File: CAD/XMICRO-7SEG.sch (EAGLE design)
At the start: 67 parts, among them U1 GAL16V8B, U10 74244, U11 74245, U2 GAL16V8B, U3 GAL16V8B, U4 GAL16V8B, U5 74273, U6 74273, U7 74138, U8 74138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

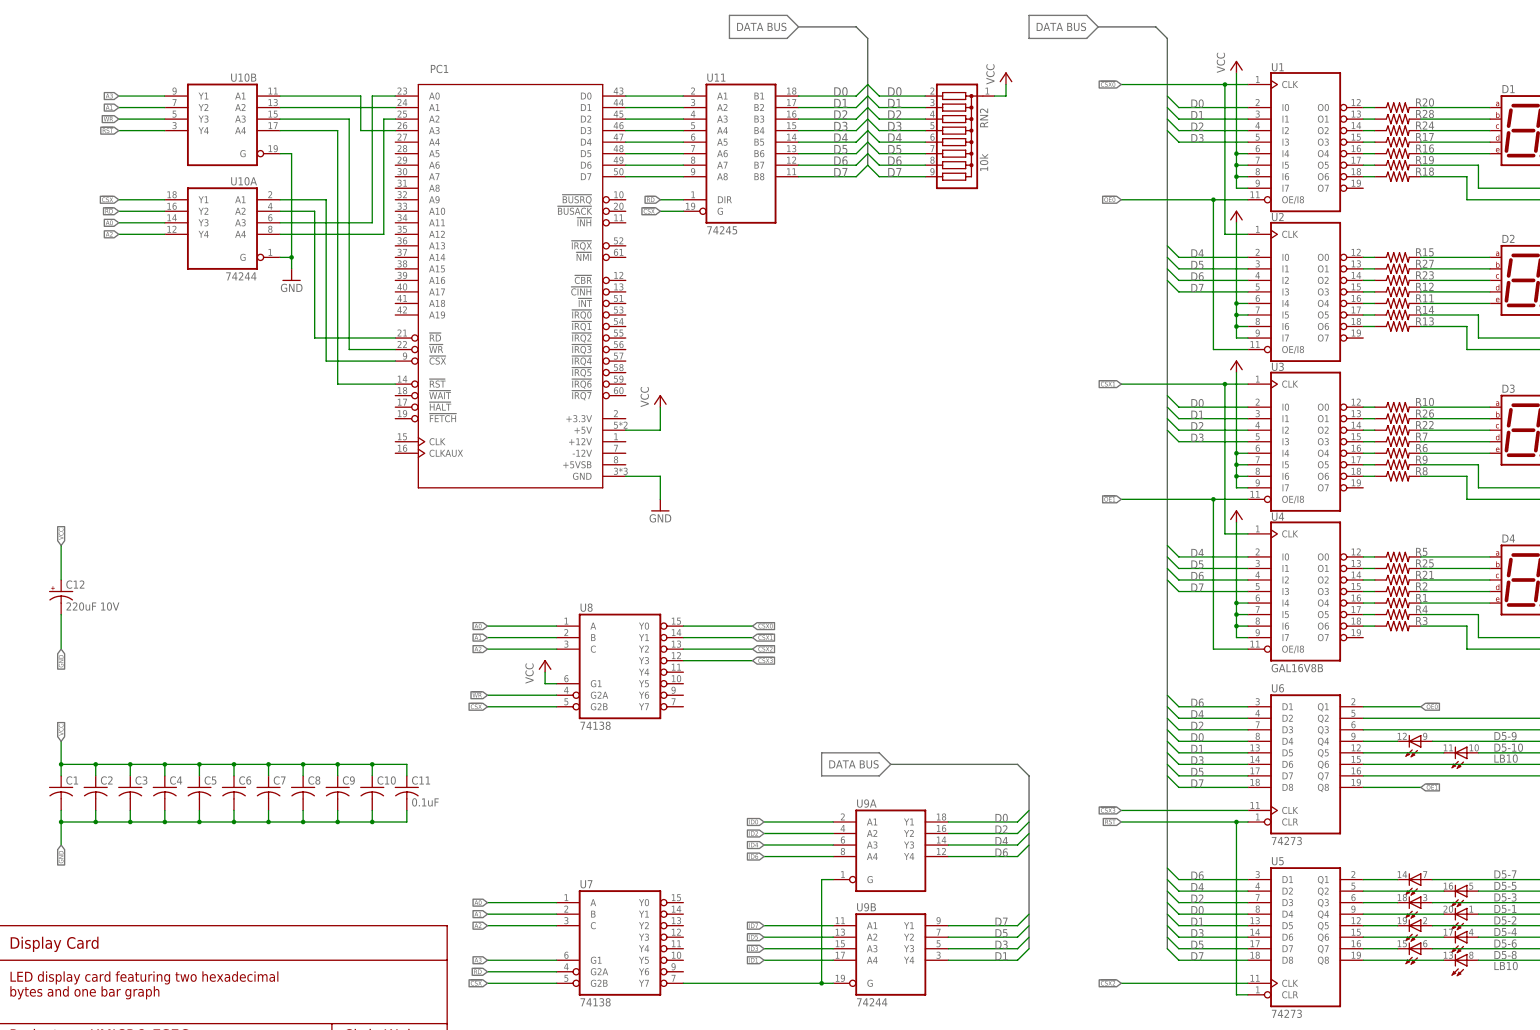
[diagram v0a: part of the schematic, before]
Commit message: Updated schematic xrefs to indicate signal direction.
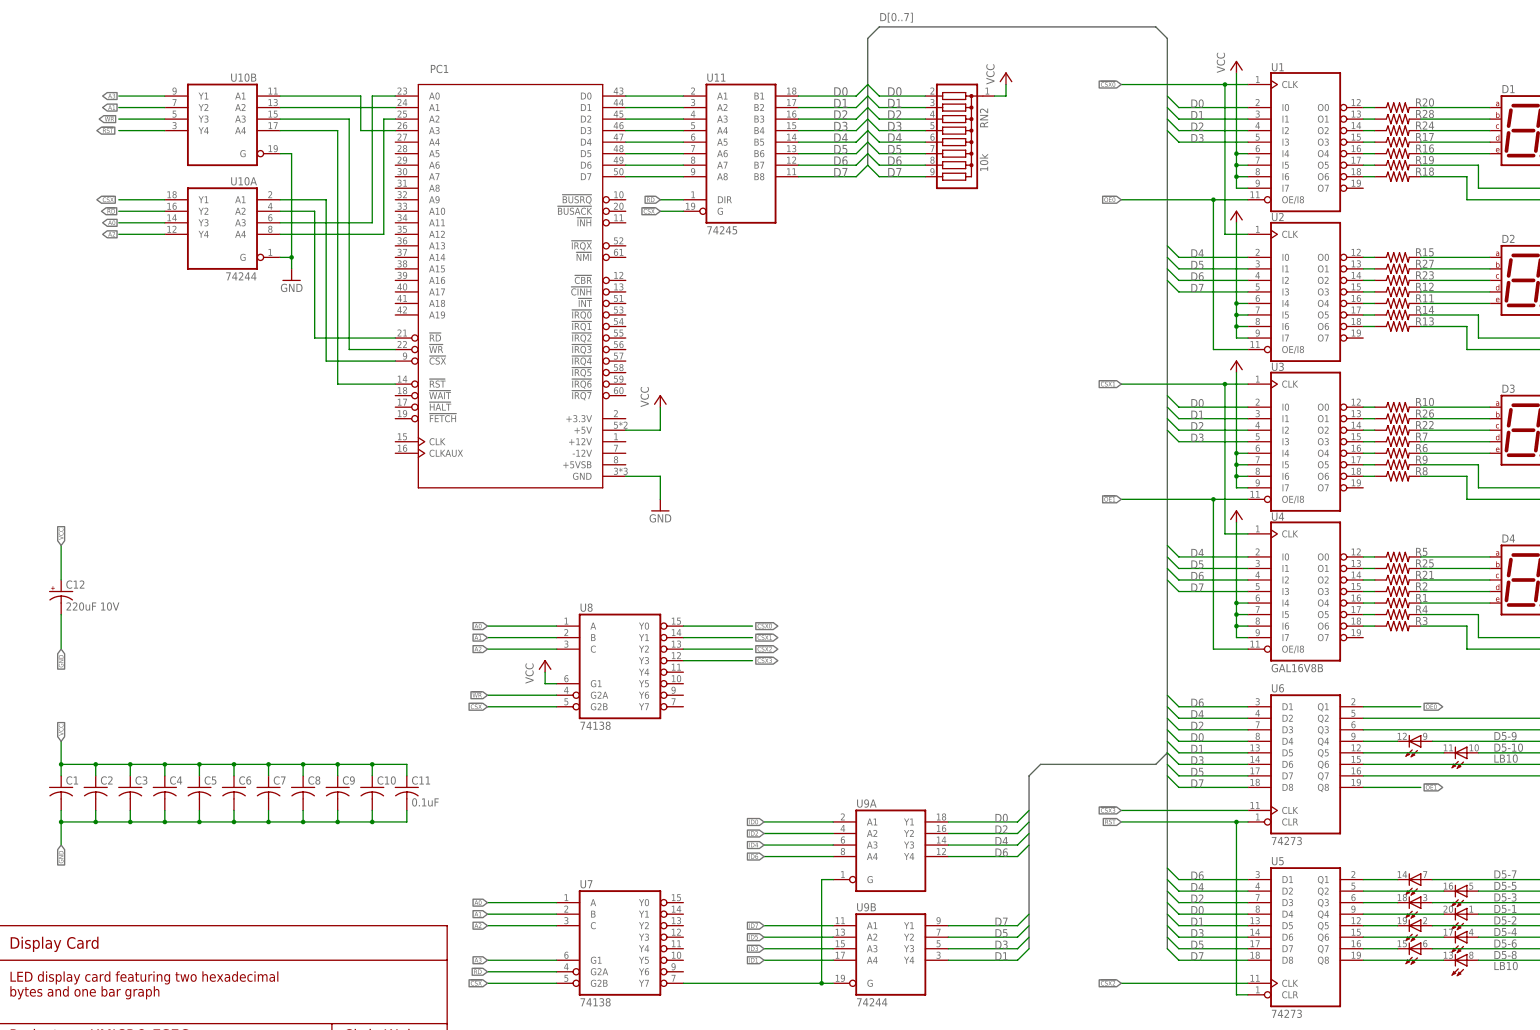
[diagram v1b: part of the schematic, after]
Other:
- note removed: "DATA BUS"
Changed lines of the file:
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@@
 <setting verticaltext="up"/>
 </settings>
-<grid distance="0.1" unitdist="inch" unit="inch" style="lines" multiple="1" display="no" altdistance="0.01" altunitdist="inch" altunit="inch"/>
+<grid distance="0.1" unitdist="inch" unit="inch" style="lines" multiple="1" display="no" altdistance="0.05" altunitdist="inch" altunit="inch"/>
 <layers>
 <layer number="1" name="Top" color="4" fill="1" visible="no" active="no"/>
@@
 <sheet>
 <plain>
-<wire x1="180.34" y1="233.68" x2="177.8" y2="231.14" width="0.1524" layer="95"/>
-<wire x1="177.8" y1="231.14" x2="165.1" y2="231.14" width="0.1524" layer="95"/>
-<wire x1="165.1" y1="231.14" x2="165.1" y2="236.22" width="0.1524" layer="95"/>
-<wire x1="165.1" y1="236.22" x2="177.8" y2="236.22" width="0.1524" layer="95"/>
-<wire x1="177.8" y1="236.22" x2="180.34" y2="233.68" width="0.1524" layer="95"/>
-<text x="177.8" y="233.68" size="1.778" layer="95" align="center-right">DATA BUS</text>
-<wire x1="246.38" y1="233.68" x2="243.84" y2="231.14" width="0.1524" layer="95"/>
-<wire x1="243.84" y1="231.14" x2="231.14" y2="231.14" width="0.1524" layer="95"/>
-<wire x1="231.14" y1="231.14" x2="231.14" y2="236.22" width="0.1524" layer="95"/>
-<wire x1="231.14" y1="236.22" x2="243.84" y2="236.22" width="0.1524" layer="95"/>
-<wire x1="243.84" y1="236.22" x2="246.38" y2="233.68" width="0.1524" layer="95"/>
-<text x="243.84" y="233.68" size="1.778" layer="95" align="center-right">DATA BUS</text>
-<wire x1="200.66" y1="71.12" x2="198.12" y2="68.58" width="0.1524" layer="95"/>
-<wire x1="198.12" y1="68.58" x2="185.42" y2="68.58" width="0.1524" layer="95"/>
-<wire x1="185.42" y1="68.58" x2="185.42" y2="73.66" width="0.1524" layer="95"/>
-<wire x1="185.42" y1="73.66" x2="198.12" y2="73.66" width="0.1524" layer="95"/>
-<wire x1="198.12" y1="73.66" x2="200.66" y2="71.12" width="0.1524" layer="95"/>
-<text x="198.12" y="71.12" size="1.778" layer="95" align="center-right">DATA BUS</text>
 <frame x1="0" y1="0" x2="406.4" y2="254" columns="8" rows="5" layer="94"/>
 <text x="6.35" y="30.48" size="2.54" layer="94" font="vector">Display Card</text>
@@
 <bus name="D[0..7]">
 <segment>
-<wire x1="193.04" y1="233.68" x2="180.34" y2="233.68" width="0.762" layer="92"/>
-<wire x1="193.04" y1="233.68" x2="195.58" y2="231.14" width="0.762" layer="92"/>
 <wire x1="195.58" y1="231.14" x2="195.58" y2="203.2" width="0.762" layer="92"/>
-</segment>
-<segment>
-<wire x1="259.08" y1="233.68" x2="246.38" y2="233.68" width="0.762" layer="92"/>
+<wire x1="195.58" y1="231.14" x2="198.12" y2="233.68" width="0.762" layer="92"/>
+<wire x1="231.14" y1="68.58" x2="231.14" y2="30.48" width="0.762" layer="92"/>
+<wire x1="231.14" y1="68.58" x2="233.68" y2="71.12" width="0.762" layer="92"/>
 <wire x1="259.08" y1="233.68" x2="261.62" y2="231.14" width="0.762" layer="92"/>
-<wire x1="261.62" y1="231.14" x2="261.62" y2="30.48" width="0.762" layer="92"/>
-</segment>
-<segment>
-<wire x1="228.6" y1="71.12" x2="200.66" y2="71.12" width="0.762" layer="92"/>
-<wire x1="228.6" y1="71.12" x2="231.14" y2="68.58" width="0.762" layer="92"/>
-<wire x1="231.14" y1="68.58" x2="231.14" y2="30.48" width="0.762" layer="92"/>
+<wire x1="261.62" y1="231.14" x2="261.62" y2="73.66" width="0.762" layer="92"/>
+<wire x1="261.62" y1="73.66" x2="261.62" y2="30.48" width="0.762" layer="92"/>
+<wire x1="233.68" y1="71.12" x2="259.08" y2="71.12" width="0.762" layer="92"/>
+<wire x1="259.08" y1="71.12" x2="261.62" y2="73.66" width="0.762" layer="92"/>
+<wire x1="198.12" y1="233.68" x2="259.08" y2="233.68" width="0.762" layer="92"/>
+<label x="198.12" y="234.95" size="1.778" layer="95"/>
 </segment>
 </bus>
@@
 <pinref part="U10" gate="A" pin="Y4"/>
 <wire x1="40.64" y1="187.96" x2="30.48" y2="187.96" width="0.1524" layer="91"/>
-<label x="30.48" y="187.96" size="1.016" layer="95" rot="R180" xref="yes"/>
+<label x="26.924" y="187.96" size="1.016" layer="95" xref="yes"/>
 </segment>
 </net>
@@
 <pinref part="U10" gate="B" pin="Y2"/>
 <wire x1="40.64" y1="215.9" x2="30.48" y2="215.9" width="0.1524" layer="91"/>
-<label x="30.48" y="215.9" size="1.016" layer="95" rot="R180" xref="yes"/>
+<label x="26.924" y="215.9" size="1.016" layer="95" xref="yes"/>
 </segment>
 </net>
@@
 <pinref part="U10" gate="A" pin="Y3"/>
 <wire x1="40.64" y1="190.5" x2="30.48" y2="190.5" width="0.1524" layer="91"/>
-<label x="30.48" y="190.5" size="1.016" layer="95" rot="R180" xref="yes"/>
+<label x="26.924" y="190.5" size="1.016" layer="95" xref="yes"/>
 </segment>
 </net>
@@
 <pinref part="U10" gate="A" pin="Y2"/>
 <wire x1="40.64" y1="193.04" x2="30.48" y2="193.04" width="0.1524" layer="91"/>
-<label x="30.48" y="193.04" size="1.016" layer="95" rot="R180" xref="yes"/>
+<label x="26.67" y="193.04" size="1.016" layer="95" xref="yes"/>
 </segment>
 </net>
@@
 <pinref part="U10" gate="B" pin="Y3"/>
 <wire x1="40.64" y1="213.36" x2="30.48" y2="213.36" width="0.1524" layer="91"/>
-<label x="30.48" y="213.36" size="1.016" layer="95" rot="R180" xref="yes"/>
+<label x="26.162" y="213.36" size="1.016" layer="95" xref="yes"/>
 </segment>
 </net>
@@
 <pinref part="U10" gate="A" pin="Y1"/>
 <wire x1="40.64" y1="195.58" x2="30.48" y2="195.58" width="0.1524" layer="91"/>
-<label x="30.48" y="195.58" size="1.016" layer="95" rot="R180" xref="yes"/>
+<label x="25.654" y="195.58" size="1.016" layer="95" xref="yes"/>
 </segment>
 </net>
@@
 <pinref part="U8" gate="A" pin="Y0"/>
 <wire x1="154.94" y1="101.6" x2="170.18" y2="101.6" width="0.1524" layer="91"/>
-<label x="170.18" y="101.6" size="1.016" layer="95" xref="yes"/>
+<label x="175.768" y="101.6" size="1.016" layer="95" rot="R180" xref="yes"/>
 </segment>
 <segment>
@@
 <pinref part="U8" gate="A" pin="Y1"/>
 <wire x1="154.94" y1="99.06" x2="170.18" y2="99.06" width="0.1524" layer="91"/>
-<label x="170.18" y="99.06" size="1.016" layer="95" xref="yes"/>
+<label x="175.768" y="99.06" size="1.016" layer="95" rot="R180" xref="yes"/>
 </segment>
 <segment>
@@
 <pinref part="U8" gate="A" pin="Y2"/>
 <wire x1="154.94" y1="96.52" x2="170.18" y2="96.52" width="0.1524" layer="91"/>
-<label x="170.18" y="96.52" size="1.016" layer="95" xref="yes"/>
+<label x="175.768" y="96.52" size="1.016" layer="95" rot="R180" xref="yes"/>
 </segment>
 <segment>
@@
 <pinref part="U8" gate="A" pin="Y3"/>
 <wire x1="154.94" y1="93.98" x2="170.18" y2="93.98" width="0.1524" layer="91"/>
-<label x="170.18" y="93.98" size="1.016" layer="95" xref="yes"/>
+<label x="175.768" y="93.98" size="1.016" layer="95" rot="R180" xref="yes"/>
 </segment>
 <segment>
@@
 <pinref part="U6" gate="A" pin="Q8"/>
 <wire x1="304.8" y1="66.04" x2="317.5" y2="66.04" width="0.1524" layer="91"/>
-<label x="317.5" y="66.04" size="1.016" layer="95" xref="yes"/>
+<label x="322.326" y="66.04" size="1.016" layer="95" rot="R180" xref="yes"/>
 </segment>
 </net>
@@
 <pinref part="U6" gate="A" pin="Q1"/>
 <wire x1="304.8" y1="83.82" x2="317.5" y2="83.82" width="0.1524" layer="91"/>
-<label x="317.5" y="83.82" size="1.016" layer="95" xref="yes"/>
+<label x="322.326" y="83.82" size="1.016" layer="95" rot="R180" xref="yes"/>
 </segment>
 </net>
@@
 <pinref part="U10" gate="B" pin="Y1"/>
 <wire x1="40.64" y1="218.44" x2="30.48" y2="218.44" width="0.1524" layer="91"/>
-<label x="30.48" y="218.44" size="1.016" layer="95" rot="R180" xref="yes"/>
+<label x="26.924" y="218.44" size="1.016" layer="95" xref="yes"/>
 </segment>
 </net>
@@
 <pinref part="U10" gate="B" pin="Y4"/>
 <wire x1="40.64" y1="210.82" x2="30.48" y2="210.82" width="0.1524" layer="91"/>
-<label x="30.48" y="210.82" size="1.016" layer="95" rot="R180" xref="yes"/>
-</segment>
-<segment>
+<label x="25.654" y="210.82" size="1.016" layer="95" xref="yes"/>
+</segment>
+<segment>
